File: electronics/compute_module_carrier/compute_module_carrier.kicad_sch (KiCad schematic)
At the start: 0 parts

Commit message: designing the compute module carrier pt.2
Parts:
- added A1: LattePanda_Mu, Module_LattePanda:LattePanda_Module_H8.0mm_Horizontal, symbol MCU_Module_LattePanda:LattePanda_Mu
- added BT1: Battery_Cell, Battery:BatteryHolder_LINX_BAT-HLD-012-SMT, symbol Device:Battery_Cell
- added R1: 1K/1%, symbol Device:R
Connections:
- new net: BT1.1 (+), R1.1
- new net GND: A1.101 (GND), A1.107 (GND), A1.11 (GND), A1.110 (GND), A1.113 (GND), A1.116 (GND), A1.135 (GND), A1.136 (GND), A1.14 (GND), A1.151 (GND), A1.158 (GND), A1.167 (GND), A1.17 (GND), A1.170 (GND), A1.181 (GND), A1.182 (GND), A1.188 (GND), A1.189 (GND), A1.194 (GND), A1.195 (GND), A1.20 (GND), A1.200 (GND), A1.201 (GND), A1.206 (GND), A1.207 (GND), A1.212 (GND), A1.213 (GND), A1.218 (GND), A1.219 (GND), A1.224 (GND), A1.225 (GND), A1.23 (GND), A1.230 (GND), A1.231 (GND), A1.236 (GND), A1.237 (GND), A1.242 (GND), A1.243 (GND), A1.248 (GND), A1.249 (GND), A1.26 (GND), A1.29 (GND), A1.32 (GND), A1.35 (GND), A1.38 (GND), A1.41 (GND), A1.44 (GND), A1.47 (GND), A1.50 (GND), A1.53 (GND), A1.56 (GND), A1.59 (GND), A1.62 (GND), A1.65 (GND), A1.68 (GND), A1.71 (GND), A1.74 (GND), A1.77 (GND), A1.80 (GND), A1.83 (GND), A1.86 (GND), A1.89 (GND), A1.92 (GND), A1.95 (GND), A1.98 (GND), A1.MP (Mounting_Pads), BT1.2 (-)
- new net VBAT: A1.115 (VBAT), R1.2
- new net VDC: A1.250 (VIN), A1.251 (VIN), A1.252 (VIN), A1.253 (VIN), A1.254 (VIN), A1.255 (VIN), A1.256 (VIN), A1.257 (VIN), A1.258 (VIN), A1.259 (VIN), A1.260 (VIN)

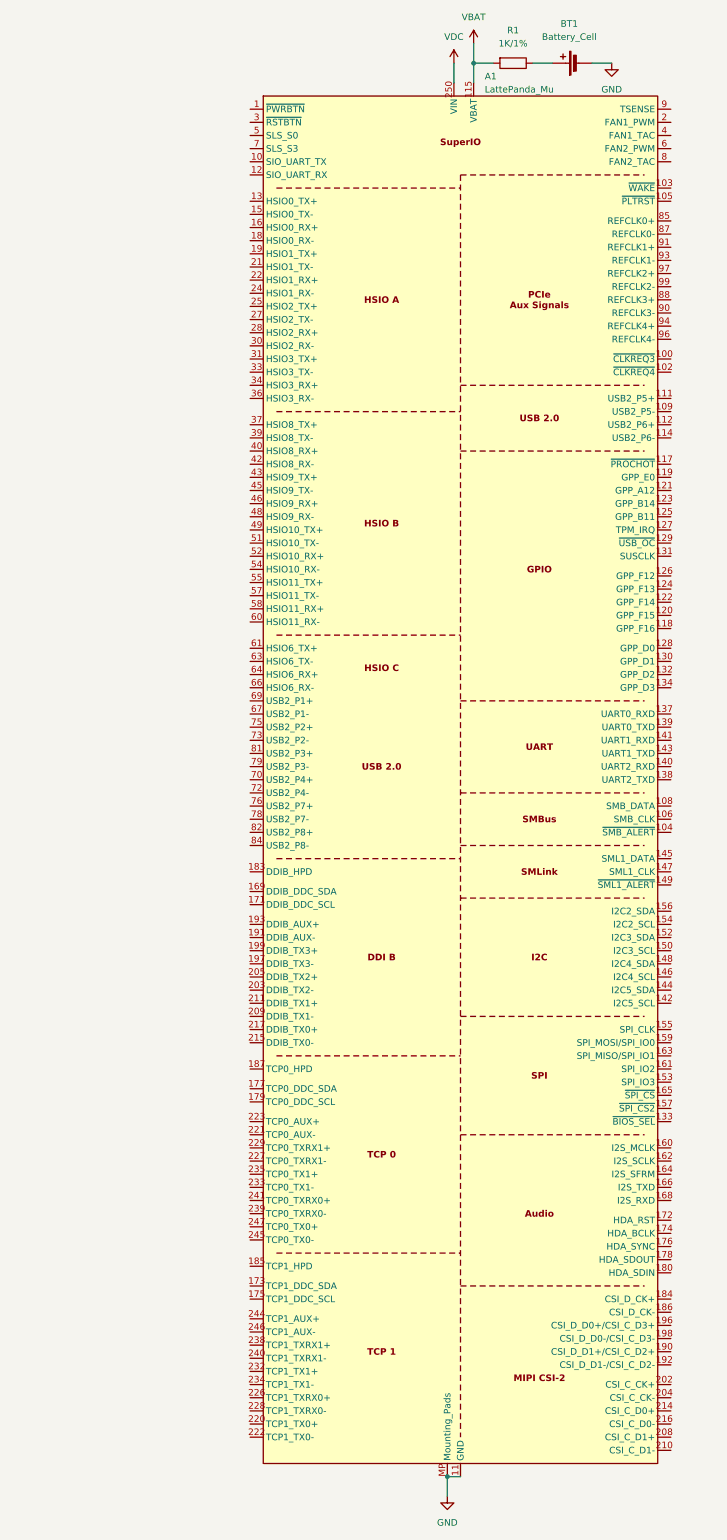
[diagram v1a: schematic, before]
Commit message: designing the compute module carrier pt.3
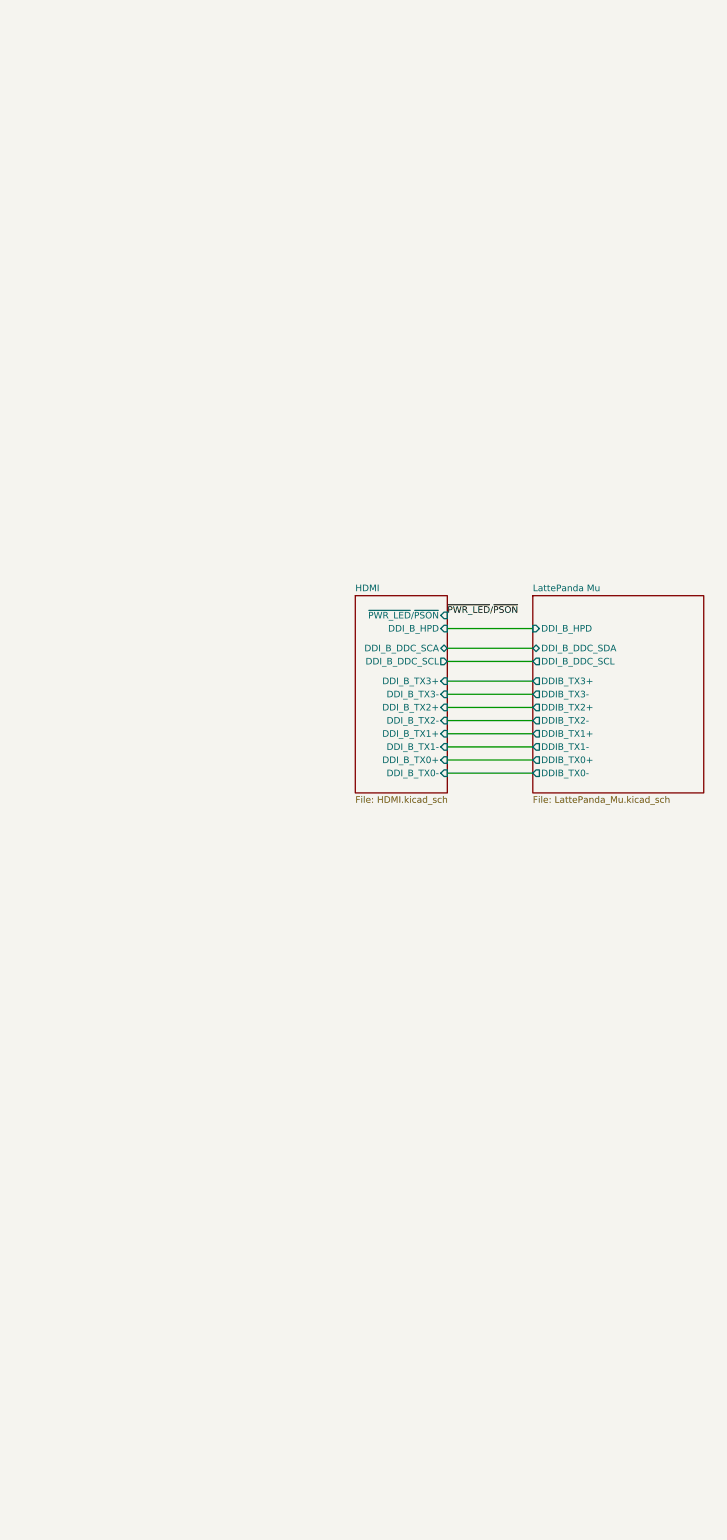
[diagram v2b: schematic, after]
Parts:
- removed A1: LattePanda_Mu, Module_LattePanda:LattePanda_Module_H8.0mm_Horizontal, symbol MCU_Module_LattePanda:LattePanda_Mu
- removed BT1: Battery_Cell, Battery:BatteryHolder_LINX_BAT-HLD-012-SMT, symbol Device:Battery_Cell
- removed R1: 1K/1%, symbol Device:R
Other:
- added sheet HDMI (HDMI.kicad_sch)
- added sheet LattePanda Mu (LattePanda_Mu.kicad_sch)

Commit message: designing the compute module carrier pt.4
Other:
- added sheet M.2 E and M Keys (M.2_E_and_M_Keys.kicad_sch)
- added sheet PCIe x4 (PCIe_x4.kicad_sch)
- sheet LattePanda Mu ports: added HSIO_2_RX+, HSIO_2_RX-, HSIO_2_TX+, HSIO_2_TX-, HSIO_3_RX+, HSIO_3_RX-, HSIO_3_TX+, HSIO_3_TX-, REFCLK0+, REFCLK0-, REFCLK3+, REFCLK3-, SUSCLK_WIFI, USB_2_P7+, USB_2_P7-, ~{CLKREQ3}; removed none

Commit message: designing the compute module carrier pt.5
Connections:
- no-connect marks 0 -> 1
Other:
- added sheet Gigabit Ethernet (Gigabit_Ethernet.kicad_sch)
- sheet LattePanda Mu ports: added HSIO_10_RX+, HSIO_10_RX-, HSIO_10_TX+, HSIO_10_TX-, HSIO_11_RX+, HSIO_11_RX-, HSIO_11_TX+, HSIO_11_TX-, HSIO_6_RX+, HSIO_6_RX-, HSIO_6_TX+, HSIO_6_TX-, HSIO_8_RX+, HSIO_8_RX-, HSIO_8_TX+, HSIO_8_TX-, HSIO_9_RX+, HSIO_9_RX-, HSIO_9_TX+, HSIO_9_TX-, REFCLK2+, REFCLK2-, REFCLK4+, REFCLK4-, ~{CLKREQ4}; removed none
- sheet M.2 E and M Keys ports: added ~{CLKREQE}; removed none

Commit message: designing the compute module carrier pt.6
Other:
- added sheet GPIOs (GPIOs.kicad_sch)
- added sheet USB3.0 (USB3.kicad_sch)
- sheet LattePanda Mu ports: added HSIO_0_RX+, HSIO_0_RX-, HSIO_0_TX+, HSIO_0_TX-, HSIO_1_RX+, HSIO_1_RX-, HSIO_1_TX+, HSIO_1_TX-, I2C2_SCL, I2C2_SDA, I2C3_SCL, I2C3_SDA, I2C4_SCL, I2C4_SDA, I2C5_SCL, I2C5_SDA, SOC_UART0_RX, SOC_UART0_TX, SOC_UART1_RX, SOC_UART1_TX, SOC_UART2_RX, SOC_UART2_TX, USB_2_P1+, USB_2_P1-, USB_2_P2+, USB_2_P2-; removed none
